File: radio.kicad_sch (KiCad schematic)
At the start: 1 part, among them U2 CC1101

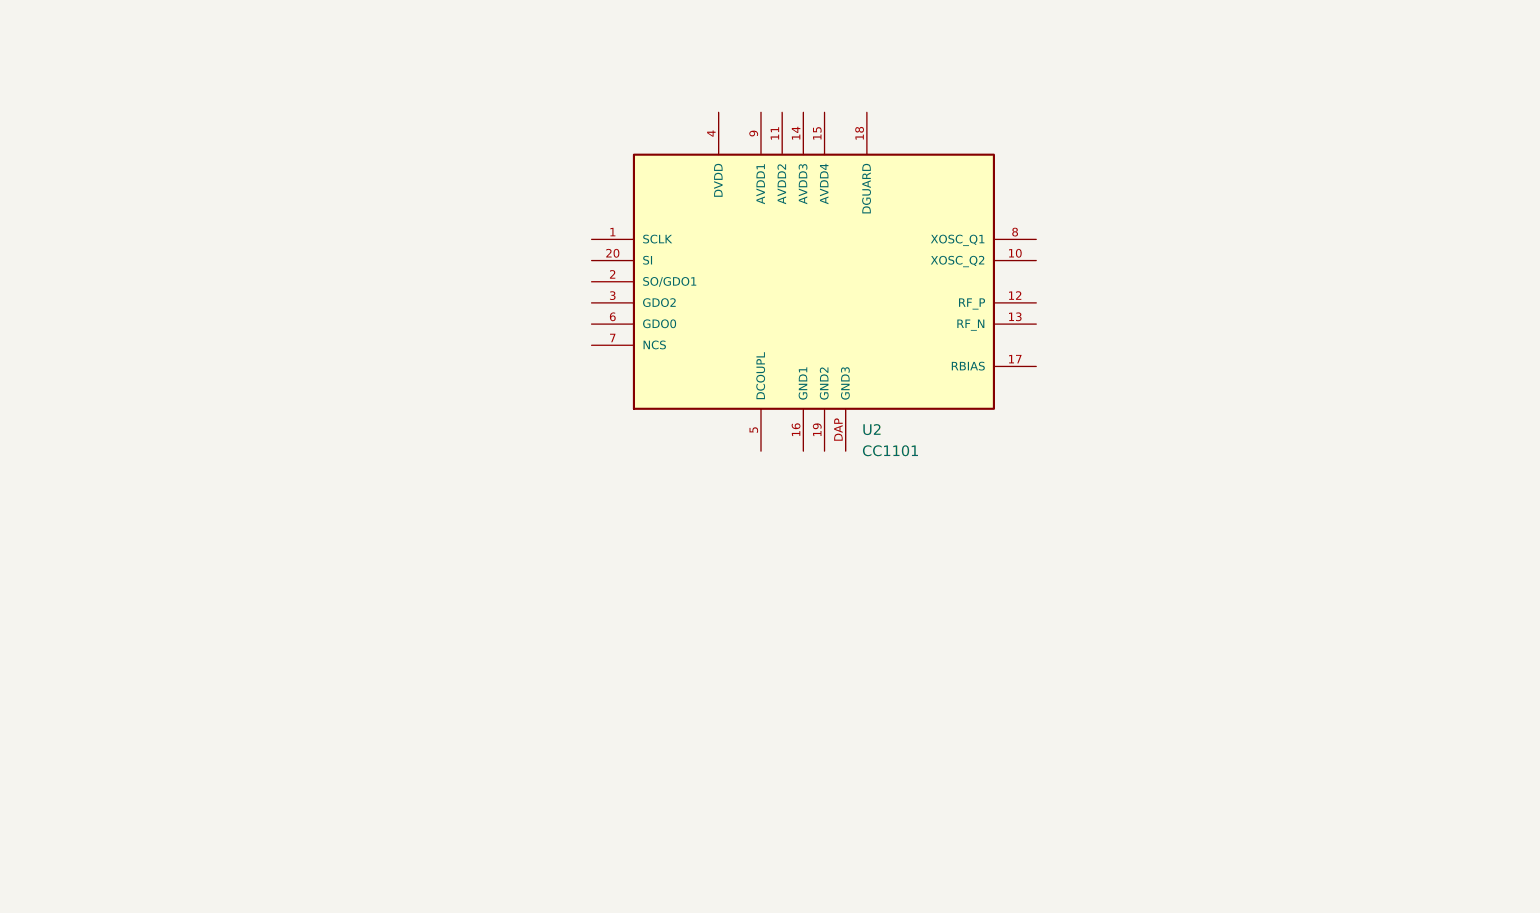
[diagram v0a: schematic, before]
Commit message: component placement inside schematic
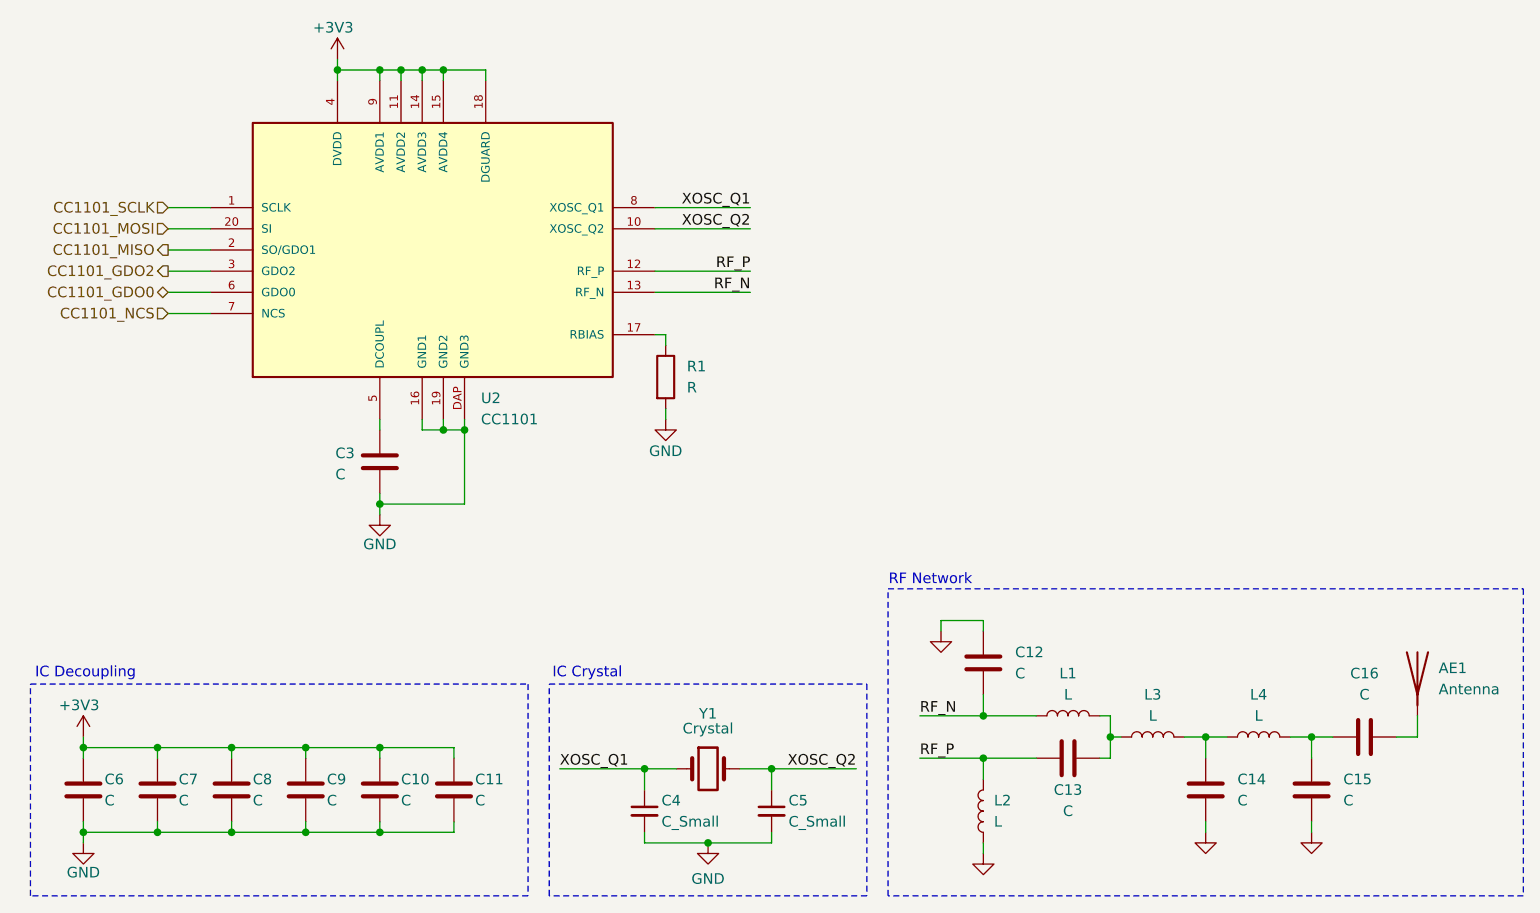
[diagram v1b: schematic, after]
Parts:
- added AE1: Antenna, symbol Device:Antenna
- added C10, C11, C12, C13, C14, C15, C16, C3, C6, C7, C8, C9: C, symbol Device:C
- added C4, C5: C_Small, symbol Device:C_Small
- added L1, L2, L3, L4: L, symbol Device:L
- added R1: R, symbol Device:R
- added Y1: Crystal, symbol Device:Crystal
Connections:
- net CC1101_SCLK: now reaches U2.1 (SCLK)
- net XOSC_Q2: now reaches U2.10 (XOSC_Q2)
- net XOSC_Q2: now also C5.1, Y1.2
- net +3V3: now reaches U2.11 (AVDD2)
- net +3V3: now also U2.14 (AVDD3), U2.15 (AVDD4), U2.18 (DGUARD), U2.4 (DVDD), U2.9 (AVDD1), C10.1, C11.1, C6.1, C7.1, C8.1, C9.1
- net RF_P: now reaches U2.12 (RF_P)
- net RF_P: now also C13.1, L2.2
- net RF_N: now reaches U2.13 (RF_N)
- net RF_N: now also C12.2, L1.1
- net GND: now reaches U2.16 (GND1)
- net GND: now also U2.19 (GND2), U2.DAP (GND3), C10.2, C11.2, C12.1, C14.2, C15.2, C3.2, C4.2, C5.2, C6.2, C7.2, C8.2, C9.2, L2.1, R1.2
- net at U2.17 (RBIAS): now also R1.1
- net CC1101_MISO: now reaches U2.2 (SO/GDO1)
- net CC1101_MOSI: now reaches U2.20 (SI)
- net CC1101_GDO2: now reaches U2.3 (GDO2)
- net at U2.5 (DCOUPL): now also C3.1
- net CC1101_GDO0: now reaches U2.6 (GDO0)
- net CC1101_NCS: now reaches U2.7 (NCS)
- net XOSC_Q1: now reaches U2.8 (XOSC_Q1)
- net XOSC_Q1: now also C4.1, Y1.1
- new net: C15.1, C16.1, L4.2
- new net: C14.1, L3.2, L4.1
- new net: AE1.1 (A), C16.2
- new net: C13.2, L1.2, L3.1
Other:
- note added: "IC Crystal"
- note added: "IC Decoupling"
- note added: "RF Network"
- moved on the sheet: U2

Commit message: set initial component footprints
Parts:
- C10: renamed from C9; footprint (none) -> Capacitor_SMD:C_0603_1608Metric
- C11: renamed from C3; footprint (none) -> Capacitor_SMD:C_0603_1608Metric
- C12: renamed from C10; footprint (none) -> Capacitor_SMD:C_0603_1608Metric
- C13: renamed from C11; footprint (none) -> Capacitor_SMD:C_0603_1608Metric
- C14: renamed from C4; footprint (none) -> Capacitor_SMD:C_0603_1608Metric
- C15: renamed from C5; footprint (none) -> Capacitor_SMD:C_0603_1608Metric
- C16: renamed from C12; footprint (none) -> Capacitor_SMD:C_0603_1608Metric
- C17: renamed from C13; footprint (none) -> Capacitor_SMD:C_0603_1608Metric
- C18: renamed from C14; footprint (none) -> Capacitor_SMD:C_0603_1608Metric
- C19: renamed from C15; footprint (none) -> Capacitor_SMD:C_0603_1608Metric
- C20: renamed from C16; footprint (none) -> Capacitor_SMD:C_0603_1608Metric
- C7: renamed from C6; footprint (none) -> Capacitor_SMD:C_0603_1608Metric
- C8: renamed from C7; footprint (none) -> Capacitor_SMD:C_0603_1608Metric
- C9: renamed from C8; footprint (none) -> Capacitor_SMD:C_0603_1608Metric
- R12: renamed from R1; footprint (none) -> Resistor_SMD:R_0603_1608Metric
- renumbered L1 to L3, L3 to L4, L4 to L5, U2 to U5

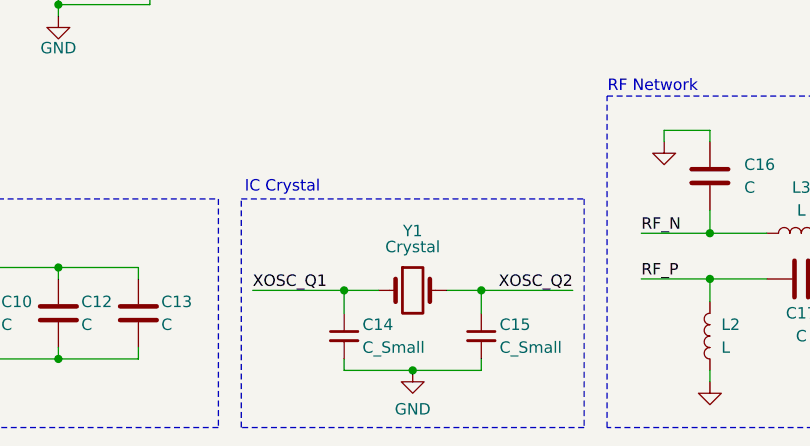
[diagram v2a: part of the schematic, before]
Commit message: Add footprints
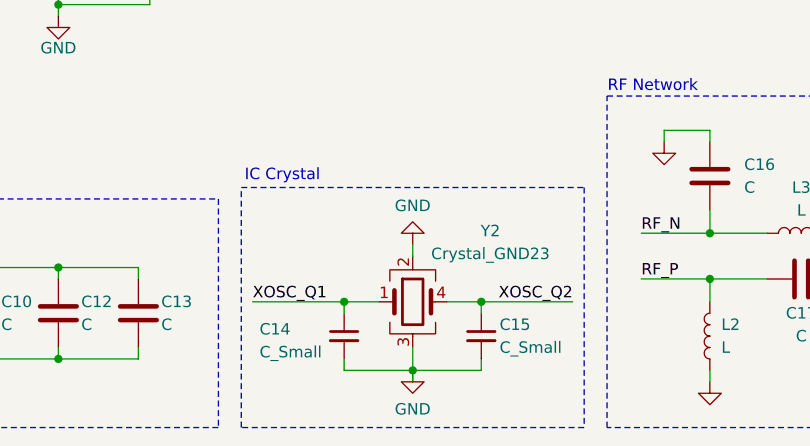
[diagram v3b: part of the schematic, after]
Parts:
- removed Y1: Crystal, symbol Device:Crystal
- added Y2: Crystal_GND23, Crystal:Crystal_SMD_3225-4Pin_3.2x2.5mm_HandSoldering, symbol Device:Crystal_GND23
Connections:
- net GND: now also Y2.2, Y2.3
- net XOSC_Q1: now also Y2.1
- net XOSC_Q2: now also Y2.4
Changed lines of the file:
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@@
 	)
 	(rectangle
-		(start 115.57 130.81)
+		(start 115.57 129.54)
 		(end 153.67 156.21)
 		(stroke
@@
 	(text "IC Crystal"
 		(exclude_from_sim no)
-		(at 120.142 129.54 0)
+		(at 120.142 128.27 0)
 		(effects
 			(font
@@
 	)
 	(junction
-		(at 142.24 140.97)
+		(at 142.24 142.24)
 		(diameter 0)
 		(color 0 0 0 0)
@@
 	)
 	(junction
-		(at 134.62 149.86)
+		(at 95.25 109.22)
 		(diameter 0)
 		(color 0 0 0 0)
 	)
 	(junction
-		(at 95.25 109.22)
+		(at 86.36 138.43)
 		(diameter 0)
 		(color 0 0 0 0)
 	)
 	(junction
-		(at 86.36 138.43)
+		(at 127 142.24)
 		(diameter 0)
 		(color 0 0 0 0)
 	)
 	(junction
-		(at 127 140.97)
+		(at 134.62 149.86)
 		(diameter 0)
 		(color 0 0 0 0)
@@
 	(wire
 		(pts
+			(xy 134.62 147.32) (xy 134.62 149.86)
+		)
+		(stroke
+			(width 0)
+			(type default)
+		)
+	)
+	(wire
+		(pts
 			(xy 90.17 57.15) (xy 95.25 57.15)
 		)
@@
 	(wire
 		(pts
-			(xy 127 143.51) (xy 127 140.97)
+			(xy 127 143.51) (xy 127 142.24)
 		)
 		(stroke
@@
 	(wire
 		(pts
-			(xy 138.43 140.97) (xy 142.24 140.97)
+			(xy 138.43 142.24) (xy 142.24 142.24)
 		)
 		(stroke
@@
 	(wire
 		(pts
+			(xy 134.62 135.89) (xy 134.62 137.16)
+		)
+		(stroke
+			(width 0)
+			(type default)
+		)
+	)
+	(wire
+		(pts
 			(xy 59.69 137.16) (xy 59.69 138.43)
 		)
@@
 	(wire
 		(pts
-			(xy 142.24 140.97) (xy 142.24 143.51)
+			(xy 142.24 142.24) (xy 142.24 143.51)
 		)
 		(stroke
@@
 	(wire
 		(pts
+			(xy 134.62 149.86) (xy 134.62 151.13)
+		)
+		(stroke
+			(width 0)
+			(type default)
+		)
+	)
+	(wire
+		(pts
 			(xy 95.25 138.43) (xy 104.14 138.43)
 		)
@@
 	(wire
 		(pts
-			(xy 142.24 140.97) (xy 152.4 140.97)
+			(xy 142.24 142.24) (xy 152.4 142.24)
 		)
 		(stroke
@@
 	(wire
 		(pts
-			(xy 127 140.97) (xy 130.81 140.97)
+			(xy 127 142.24) (xy 130.81 142.24)
 		)
 		(stroke
@@
 	(wire
 		(pts
-			(xy 116.84 140.97) (xy 127 140.97)
+			(xy 116.84 142.24) (xy 127 142.24)
 		)
 		(stroke
@@
 	)
 	(label "XOSC_Q1"
-		(at 116.84 140.97 0)
+		(at 116.84 142.24 0)
 		(effects
 			(font
@@
 	)
 	(label "XOSC_Q2"
-		(at 152.4 140.97 180)
+		(at 152.4 142.24 180)
 		(effects
 			(font
@@
 	)
 	(symbol
-		(lib_id "Device:Crystal")
-		(at 134.62 140.97 0)
-		(unit 1)
-		(exclude_from_sim no)
-		(in_bom yes)
-		(on_board yes)
-		(dnp no)
-		(property "Reference" "Y1"
-			(at 134.62 134.366 0)
-			(effects
-				(font
-					(size 1.27 1.27)
-				)
-			)
-		)
-		(property "Value" "Crystal"
-			(at 134.62 136.144 0)
-			(effects
-				(font
-					(size 1.27 1.27)
-				)
-			)
-		)
-		(property "Footprint" ""
-			(at 134.62 140.97 0)
-			(effects
-				(font
-					(size 1.27 1.27)
-				)
-				(hide yes)
-			)
-		)
-		(property "Datasheet" "~"
-			(at 134.62 140.97 0)
-			(effects
-				(font
-					(size 1.27 1.27)
-				)
-				(hide yes)
-			)
-		)
-		(property "Description" "Two pin crystal"
-			(at 134.62 140.97 0)
-			(effects
-				(font
-					(size 1.27 1.27)
-				)
-				(hide yes)
-			)
-		)
-		(pin "1"
-		)
-		(pin "2"
-		)
-		(instances
-			(project ""
-				(path "/3130e1f2-bde1-4b12-bd54-0e1e50bd36da/0d11e703-01d4-42f6-b6d1-2a98bd387429"
-					(reference "Y1")
-					(unit 1)
-				)
-			)
-		)
-	)
-	(symbol
 		(lib_id "power:GND")
 		(at 207.01 148.59 0)
@@
 		(dnp no)
 		(property "Reference" "C14"
-			(at 129.032 144.78 0)
+			(at 117.602 145.288 0)
 			(effects
 				(font
@@
 		)
 		(property "Value" "C_Small"
-			(at 129.032 147.32 0)
+			(at 117.602 147.828 0)
 			(effects
 				(font
@@
 	)
 	(symbol
+		(lib_id "power:GND")
+		(at 134.62 135.89 180)
+		(unit 1)
+		(exclude_from_sim no)
+		(in_bom yes)
+		(on_board yes)
+		(dnp no)
+		(property "Reference" "#PWR044"
+			(at 134.62 129.54 0)
+			(effects
+				(font
+					(size 1.27 1.27)
+				)
+				(hide yes)
+			)
+		)
+		(property "Value" "GND"
+			(at 134.62 131.572 0)
+			(effects
+				(font
+					(size 1.27 1.27)
+				)
+			)
+		)
+		(property "Footprint" ""
+			(at 134.62 135.89 0)
+			(effects
+				(font
+					(size 1.27 1.27)
+				)
+				(hide yes)
+			)
+		)
+		(property "Datasheet" ""
+			(at 134.62 135.89 0)
+			(effects
+				(font
+					(size 1.27 1.27)
+				)
+				(hide yes)
+			)
+		)
+		(property "Description" "Power symbol creates a global label with name \"GND\" , ground"
+			(at 134.62 135.89 0)
+			(effects
+				(font
+					(size 1.27 1.27)
+				)
+				(hide yes)
+			)
+		)
+		(pin "1"
+		)
+		(instances
+			(project "pipu-zero"
+				(path "/3130e1f2-bde1-4b12-bd54-0e1e50bd36da/0d11e703-01d4-42f6-b6d1-2a98bd387429"
+					(reference "#PWR044")
+					(unit 1)
+				)
+			)
+		)
+	)
+	(symbol
 		(lib_id "Device:C")
 		(at 194.31 143.51 0)
@@
 					(unit 1)
 				)
+			)
+		)
+	)
+	(symbol
+		(lib_id "Device:Crystal_GND23")
+		(at 134.62 142.24 0)
+		(unit 1)
+		(exclude_from_sim no)
+		(in_bom yes)
+		(on_board yes)
+		(dnp no)
+		(property "Reference" "Y2"
+			(at 143.256 134.366 0)
+			(effects
+				(font
+					(size 1.27 1.27)
+				)
+			)
+		)
+		(property "Value" "Crystal_GND23"
+			(at 143.256 136.906 0)
+			(effects
+				(font
+					(size 1.27 1.27)
+				)
+			)
+		)
+		(property "Footprint" "Crystal:Crystal_SMD_3225-4Pin_3.2x2.5mm_HandSoldering"
+			(at 134.62 142.24 0)
+			(effects
+				(font
+					(size 1.27 1.27)
+				)
+				(hide yes)
+			)
+		)
+		(property "Datasheet" "~"
+			(at 134.62 142.24 0)
+			(effects
+				(font
+					(size 1.27 1.27)
+				)
+				(hide yes)
+			)
+		)
+		(property "Description" "Four pin crystal, GND on pins 2 and 3"
+			(at 134.62 142.24 0)
+			(effects
+				(font
+					(size 1.27 1.27)
+				)
+				(hide yes)
+			)
+		)
+		(pin "4"
+		)
+		(pin "3"
+		)
+		(pin "1"
+		)
+		(pin "2"
+		)
+		(instances
+			(project ""
+				(path "/3130e1f2-bde1-4b12-bd54-0e1e50bd36da/0d11e703-01d4-42f6-b6d1-2a98bd387429"
+					(reference "Y2")
+					(unit 1)
+				)

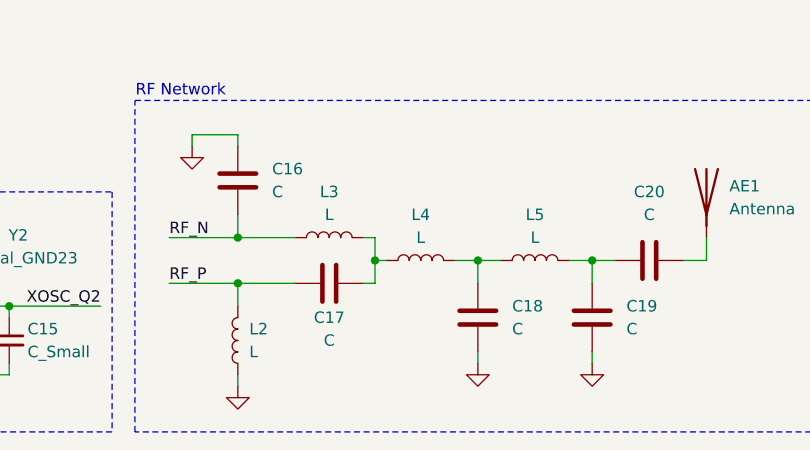
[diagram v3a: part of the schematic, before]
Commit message: Add footprints
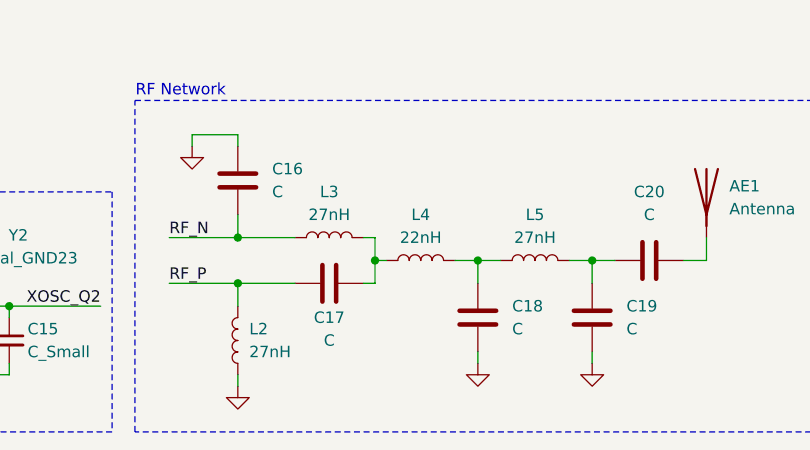
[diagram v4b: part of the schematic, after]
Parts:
- L2, L3, L5: value L -> 27nH
- L4: value L -> 22nH
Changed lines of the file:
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@@
 			)
 		)
-		(property "Value" "L"
+		(property "Value" "27nH"
 			(at 168.91 147.3199 0)
 			(effects
@@
 			)
 		)
-		(property "Value" "L"
+		(property "Value" "27nH"
 			(at 200.66 134.62 90)
 			(effects
@@
 			)
 		)
-		(property "Value" "L"
+		(property "Value" "27nH"
 			(at 177.8 132.08 90)
 			(effects
@@
 			)
 		)
-		(property "Value" "L"
+		(property "Value" "22nH"
 			(at 187.96 134.62 90)
 			(effects

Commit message: Initial pcb component placement
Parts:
- L2, L3, L4, L5: footprint (none) -> Inductor_SMD:L_0603_1608Metric
- U5: footprint CC1101:QLP20 -> cc1101:QLP20
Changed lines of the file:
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@@
 			)
 		)
-		(property "Footprint" "CC1101:QLP20"
+		(property "Footprint" "cc1101:QLP20"
 			(at 100.33 78.74 0)
 			(effects
@@
 			)
 		)
-		(property "Footprint" ""
+		(property "Footprint" "Inductor_SMD:L_0603_1608Metric"
 			(at 167.64 146.05 0)
 			(effects
@@
 			)
 		)
-		(property "Footprint" ""
+		(property "Footprint" "Inductor_SMD:L_0603_1608Metric"
 			(at 200.66 137.16 0)
 			(effects
@@
 			)
 		)
-		(property "Footprint" ""
+		(property "Footprint" "Inductor_SMD:L_0603_1608Metric"
 			(at 177.8 134.62 0)
 			(effects
@@
 			)
 		)
-		(property "Footprint" ""
+		(property "Footprint" "Inductor_SMD:L_0603_1608Metric"
 			(at 187.96 137.16 0)
 			(effects

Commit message: Add bypass capacitors
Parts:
- C10, C12, C13, C14, C15, C7, C8, C9: footprint Capacitor_SMD:C_0603_1608Metric -> Capacitor_SMD:C_0402_1005Metric
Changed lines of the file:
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@@
 			)
 		)
-		(property "Footprint" "Capacitor_SMD:C_0603_1608Metric"
+		(property "Footprint" "Capacitor_SMD:C_0402_1005Metric"
 			(at 60.6552 147.32 0)
 			(effects
@@
 			)
 		)
-		(property "Footprint" "Capacitor_SMD:C_0603_1608Metric"
+		(property "Footprint" "Capacitor_SMD:C_0402_1005Metric"
 			(at 87.3252 147.32 0)
 			(effects
@@
 			)
 		)
-		(property "Footprint" "Capacitor_SMD:C_0603_1608Metric"
+		(property "Footprint" "Capacitor_SMD:C_0402_1005Metric"
 			(at 69.5452 147.32 0)
 			(effects
@@
 			)
 		)
-		(property "Footprint" "Capacitor_SMD:C_0603_1608Metric"
+		(property "Footprint" "Capacitor_SMD:C_0402_1005Metric"
 			(at 127 146.05 0)
 			(effects
@@
 			)
 		)
-		(property "Footprint" "Capacitor_SMD:C_0603_1608Metric"
+		(property "Footprint" "Capacitor_SMD:C_0402_1005Metric"
 			(at 142.24 146.05 0)
 			(effects
@@
 			)
 		)
-		(property "Footprint" "Capacitor_SMD:C_0603_1608Metric"
+		(property "Footprint" "Capacitor_SMD:C_0402_1005Metric"
 			(at 78.4352 147.32 0)
 			(effects
@@
 			)
 		)
-		(property "Footprint" "Capacitor_SMD:C_0603_1608Metric"
+		(property "Footprint" "Capacitor_SMD:C_0402_1005Metric"
 			(at 96.2152 147.32 0)
 			(effects
@@
 			)
 		)
-		(property "Footprint" "Capacitor_SMD:C_0603_1608Metric"
+		(property "Footprint" "Capacitor_SMD:C_0402_1005Metric"
 			(at 105.1052 147.32 0)
 			(effects

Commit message: add antenna connector
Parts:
- AE1: footprint (none) -> Connector_PinHeader_2.54mm:PinHeader_1x01_P2.54mm_Vertical
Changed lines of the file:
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@@
 			)
 		)
-		(property "Footprint" ""
+		(property "Footprint" "Connector_PinHeader_2.54mm:PinHeader_1x01_P2.54mm_Vertical"
 			(at 219.71 129.54 0)
 			(effects
